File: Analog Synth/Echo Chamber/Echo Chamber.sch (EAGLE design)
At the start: 19 parts, among them IC7 78L05, IC8 TL082P

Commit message: working on the Echo Chamber schematic; PT2399 was added to \!synth_sch library
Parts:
- removed CV-A, CV-B: I/O, !synth_sch:MONO_JACK
- removed R-CV-B-ATTN: 100 kΩ, pot:TRIM_US-B64Y
- removed R23: 100 kΩ, resistor:R-US_0204/7
- added AUDIO-LVL, FEEDBACK, LED1-TRIM, LED2-TRIM1, RATE: 100 kΩ, pot:TRIM_US-B64Y
- added AUDIO_IN, ECHO_OUT: I/O, !synth_sch:MONO_JACK
- added C1, C19: 4.7 µF, rcl:C-US025-060X050
- added C13, C7: 560 pF, capacitor-wima:C5/2.5
- added C14, C15: 0.082 µF, capacitor-wima:C5/2.5
- added C16: 3300 pF, capacitor-wima:C5/2.5
- added C17: 0.01 µF, capacitor-wima:C5/2.5
- added C18, C20, C22, C23: 10 µF, rcl:C-US025-060X050
- added C2: 3900 pF, capacitor-wima:C5/2.5
- added C21, C24, C5, C6: 0.1 µF, capacitor-wima:C5/2.5
- added LED-AUDIO_IN, LED-ECHO_OUT: (no value), led:LED3MM
- added Q1, Q2: 2N3906, transistor-small-signal:2N3906
- added R1: 100 kΩ, resistor:R-US_0204/7
- added R10, R13, R7, R8, R9: 10 kΩ, resistor:R-US_0204/7
- added R11: 15 kΩ, resistor:R-US_0204/7
- added R12: 5.6 kΩ, resistor:R-US_0204/7
- added R14: 4.7 kΩ, resistor:R-US_0204/7
- added R15, R6: 2.2 kΩ, resistor:R-US_0204/7
- added R2: 18 kΩ, resistor:R-US_0204/7
- added R3: 82 kΩ, resistor:R-US_0204/7
- added R4: 1 kΩ, resistor:R-US_0204/7
- added R5: 2.7 kΩ, resistor:R-US_0204/7
- added U$1: PT2399, !synth_sch:PT2399
- C4: value 100 µF -> 4.7 µF
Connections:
- removed net 5V: C3.1, IC7.VO
- new net +5V: C23.1, C24.1, C3.1, C5.1, IC7.VO, U$1.P$1
- new net AUDIO_IN: C19.1, C2.1, C4.1, D5.C, R10.1, R7.1
- new net CV-A: AUDIO-LVL.E, IC8A.-IN, IC8A.OUT, R15.2
- new net ECHO: C1.1, C20.2
- new net N$1: C1.2, IC8B.+IN, R1.2
- new net N$10: C17.1, C18.1, R12.1
- new net N$11: C14.2, U$1.P$11
- new net N$13: C15.1, U$1.P$10
- new net N$14: C15.2, U$1.P$9
- new net N$16: C16.1, R11.1, R8.1, R9.1
- new net N$17: C20.1, R14.1
- new net N$18: C13.1, R11.2, R12.2, U$1.P$14
- new net N$19: C18.2, FEEDBACK.E
- new net N$2: IC8B.-IN, R2.2, R3.1
- new net N$22: FEEDBACK.S, R13.2
- new net N$23: C19.2, R13.1
- new net N$24: C6.2, U$1.P$7
- new net N$25: C21.1, U$1.P$8
- new net N$26: LED-ECHO_OUT.C, Q2.E
- new net N$27: LED-AUDIO_IN.A, R15.1
- new net N$28: R5.1, U$1.P$6
- new net N$29: R5.2, RATE.S
- new net N$3: IC8B.OUT, R3.2, R4.1, R6.2
- new net N$30: LED-ECHO_OUT.A, R6.1
- new net N$31: LED2-TRIM1.S, Q2.B
- new net N$34: LED1-TRIM.S, Q1.B
- new net N$5: ECHO_OUT.P2, ECHO_OUT.P3, R4.2
- new net N$6: C7.1, R7.2, U$1.P$16
- new net N$7: C7.2, R10.2, R14.2, U$1.P$15
- new net N$8: C13.2, R9.2, U$1.P$13
- new net N$9: C14.1, R8.2, U$1.P$12
- net GND: now also AUDIO-LVL.A, AUDIO_IN.P$1, AUDIO_IN.P3, C16.2, C17.2, C2.2, C21.2, C22.2, C23.2, C24.2, C5.2, C6.1, ECHO_OUT.P$1, FEEDBACK.A, LED1-TRIM.E, LED2-TRIM1.E, R1.1, R2.1, RATE.A, U$1.P$3, U$1.P$4; no longer CV-A.P$1, CV-A.P3, R-CV-B-ATTN.A
- net N$15: now also AUDIO_IN.P2; no longer CV-A.P2
- net N$21: now also AUDIO-LVL.S; no longer R-CV-B-ATTN.S
- net N$33: now also C22.1, U$1.P$2; no longer C4.1, D5.C
- net N$4: now also LED-AUDIO_IN.C, Q1.E; no longer IC8A.-IN, IC8A.OUT, R-CV-B-ATTN.E
- net V-: now also LED1-TRIM.A, LED2-TRIM1.A, Q2.C

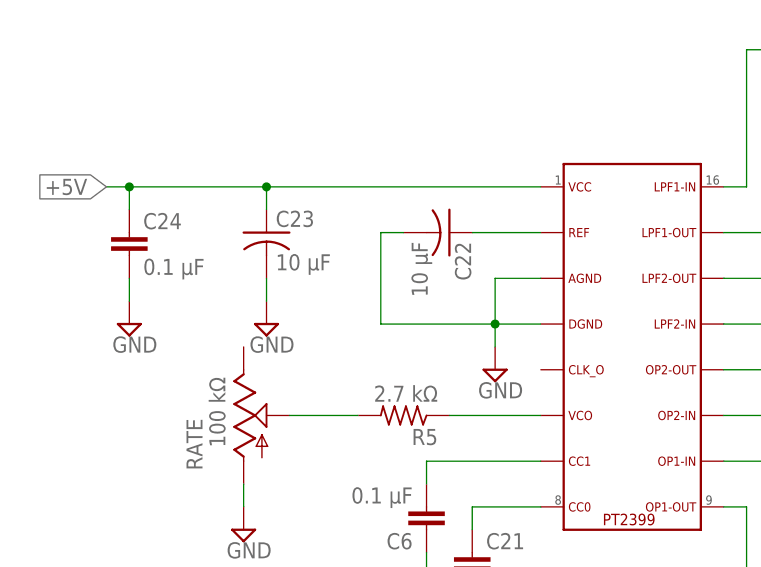
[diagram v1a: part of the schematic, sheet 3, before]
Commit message: fixed little bug with the Echo Chamber schematic
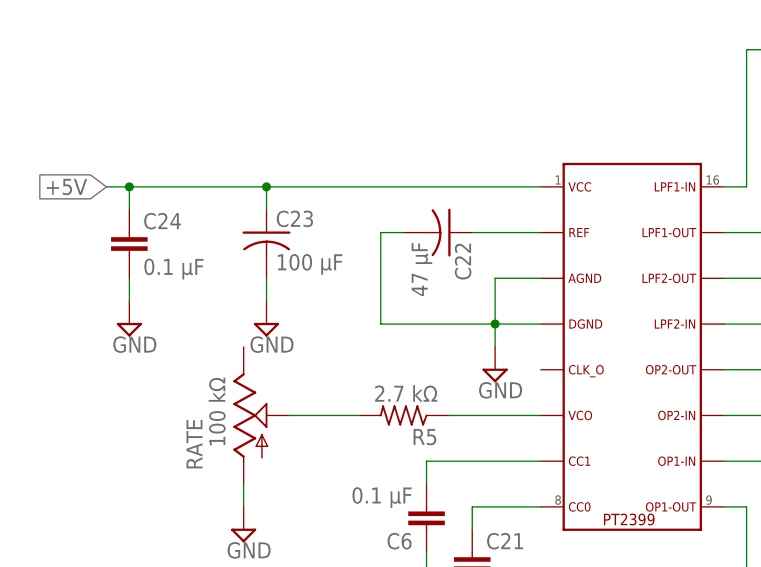
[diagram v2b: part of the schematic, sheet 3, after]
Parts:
- C22: value 10 µF -> 47 µF
- C23: value 10 µF -> 100 µF
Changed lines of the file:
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@@
 <part name="SUPPLY13" library="supply2" deviceset="GND" device=""/>
 <part name="SUPPLY14" library="supply2" deviceset="GND" device=""/>
-<part name="C22" library="rcl" deviceset="C-US" device="025-060X050" value="10 µF"/>
-<part name="C23" library="rcl" deviceset="C-US" device="025-060X050" value="10 µF"/>
+<part name="C22" library="rcl" deviceset="C-US" device="025-060X050" value="47 µF"/>
+<part name="C23" library="rcl" deviceset="C-US" device="025-060X050" value="100 µF"/>
 <part name="C24" library="capacitor-wima" deviceset="C" device="5/2.5" value="0.1 µF"/>
 <part name="SUPPLY15" library="supply2" deviceset="GND" device=""/>

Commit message: added some guide information to the schematic for the LEDs and the diodes, as well as referencing the data sheet as the source of the basic design of the PT2399 circuit
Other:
- note added: "D5 is to prevent C4 from accumulating a large reverse-voltage. Under normal conditions, D5 should never turn on."
- note added: "LED1-TRIM and LED2-TRIM should be adjusted so that the LEDs have just turned completely off when there is no audio. These need not be multi-turn potentiometers."
- note added: "This circuit was modified from the original example circuit from the PT2399 data sheet"
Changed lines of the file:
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@@
 <description>Audio In/Out</description>
 <plain>
+<text x="15.24" y="50.8" size="1.778" layer="98">LED1-TRIM and LED2-TRIM should be adjusted
+so that the LEDs have just turned completely
+off when there is no audio. These need not be
+multi-turn potentiometers.</text>
+<text x="-66.04" y="53.34" size="1.778" layer="98">D5 is to prevent C4 from accumulating a large
+reverse-voltage. Under normal conditions, D5
+should never turn on.</text>
 </plain>
 <instances>
@@
 <description>Echo Module</description>
 <plain>
+<text x="-55.88" y="76.2" size="1.778" layer="98">This circuit was modified from the original
+example circuit from the PT2399 data sheet</text>
 </plain>
 <instances>
@@
 </schematic>
 </drawing>
+<compatibility>
+<note version="6.3" minversion="6.2.2" severity="warning">
+Since Version 6.2.2 text objects can contain more than one line,
+which will not be processed correctly with this version.
+</note>
+</compatibility>
 </eagle>
